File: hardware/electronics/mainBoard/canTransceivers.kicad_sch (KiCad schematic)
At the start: 20 parts, among them U6 TCAN3403-Q1, U7 TCAN3403-Q1

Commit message: assigned FPs
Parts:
- U6, U7: footprint (none) -> lib_ICs:SON65P300X300X100-8
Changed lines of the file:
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@@
 			)
 		)
-		(property "Footprint" ""
+		(property "Footprint" "lib_ICs:SON65P300X300X100-8"
 			(at 139.7 63.5 0)
 			(effects
@@
 			)
 		)
-		(property "Footprint" ""
+		(property "Footprint" "lib_ICs:SON65P300X300X100-8"
 			(at 139.7 127 0)
 			(effects

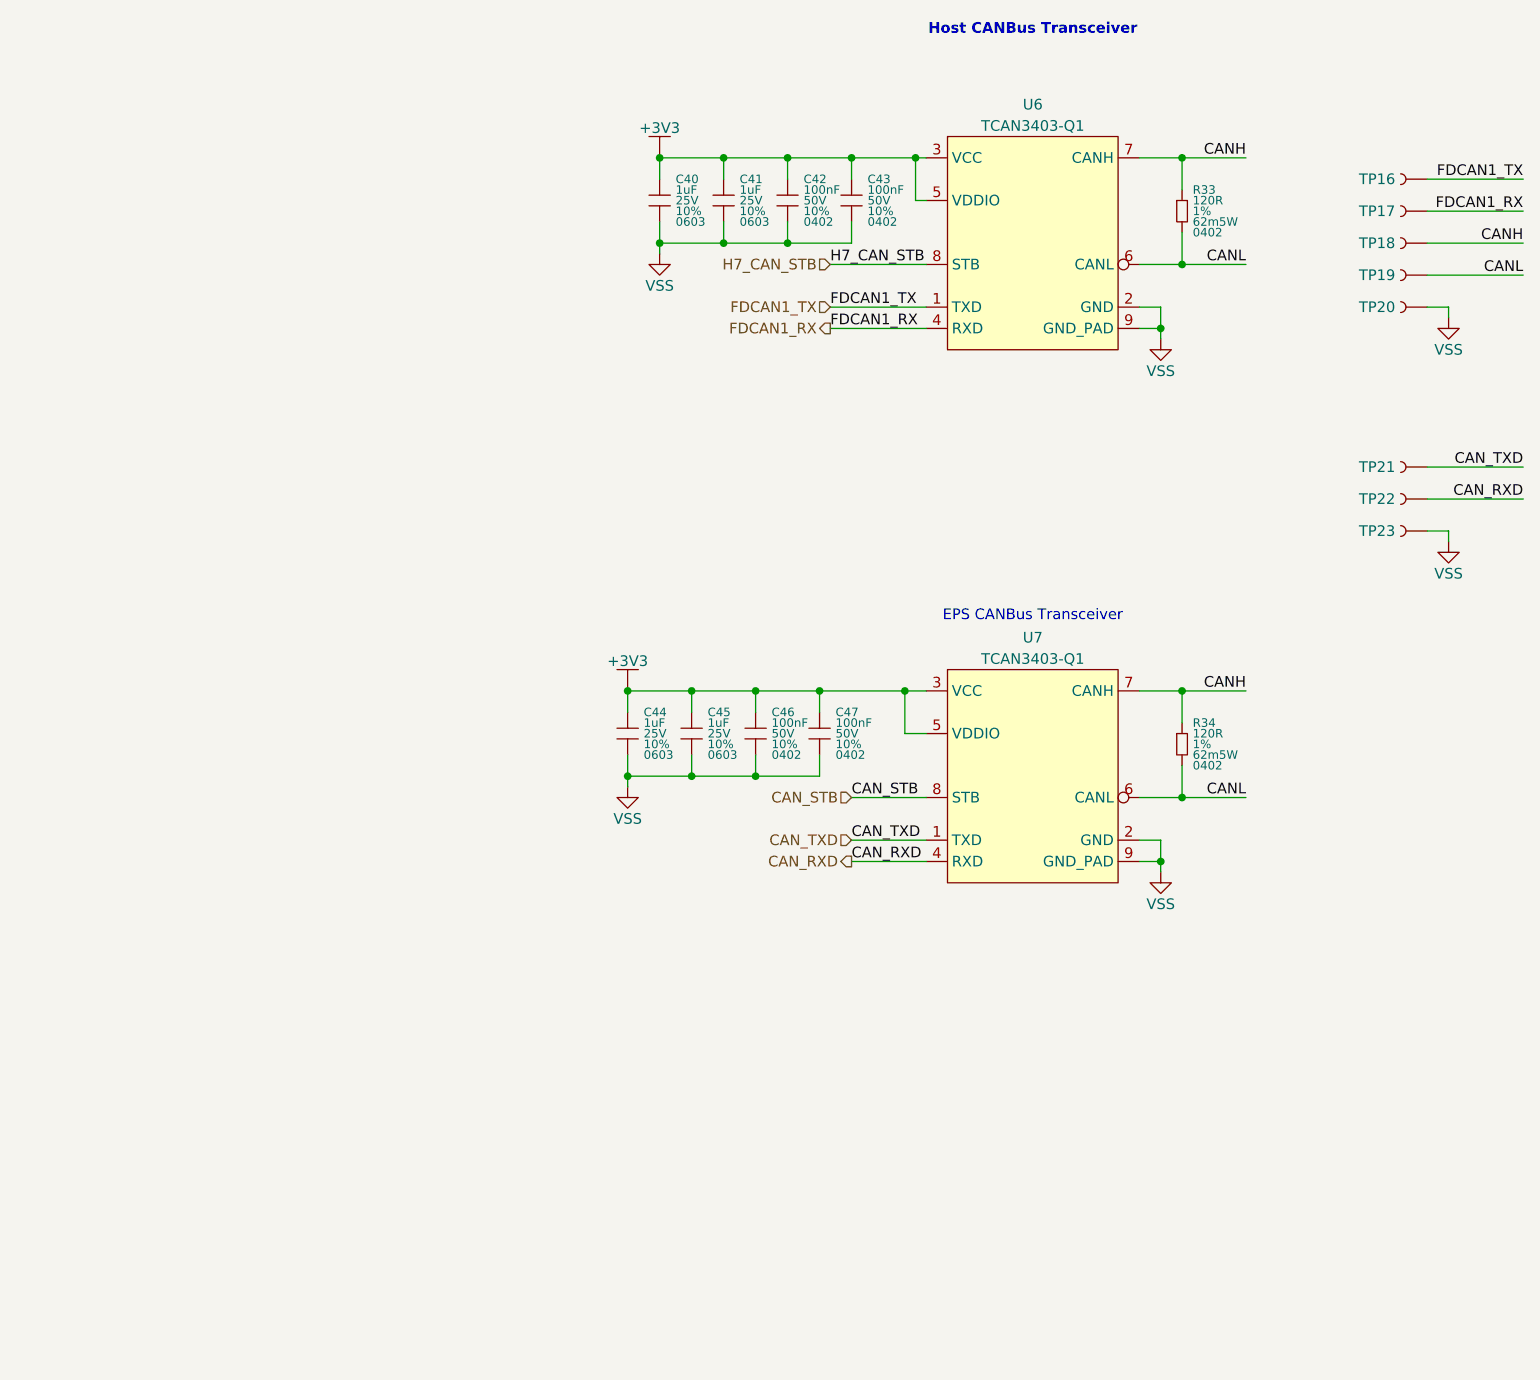
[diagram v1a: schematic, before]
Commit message: assigned footprints
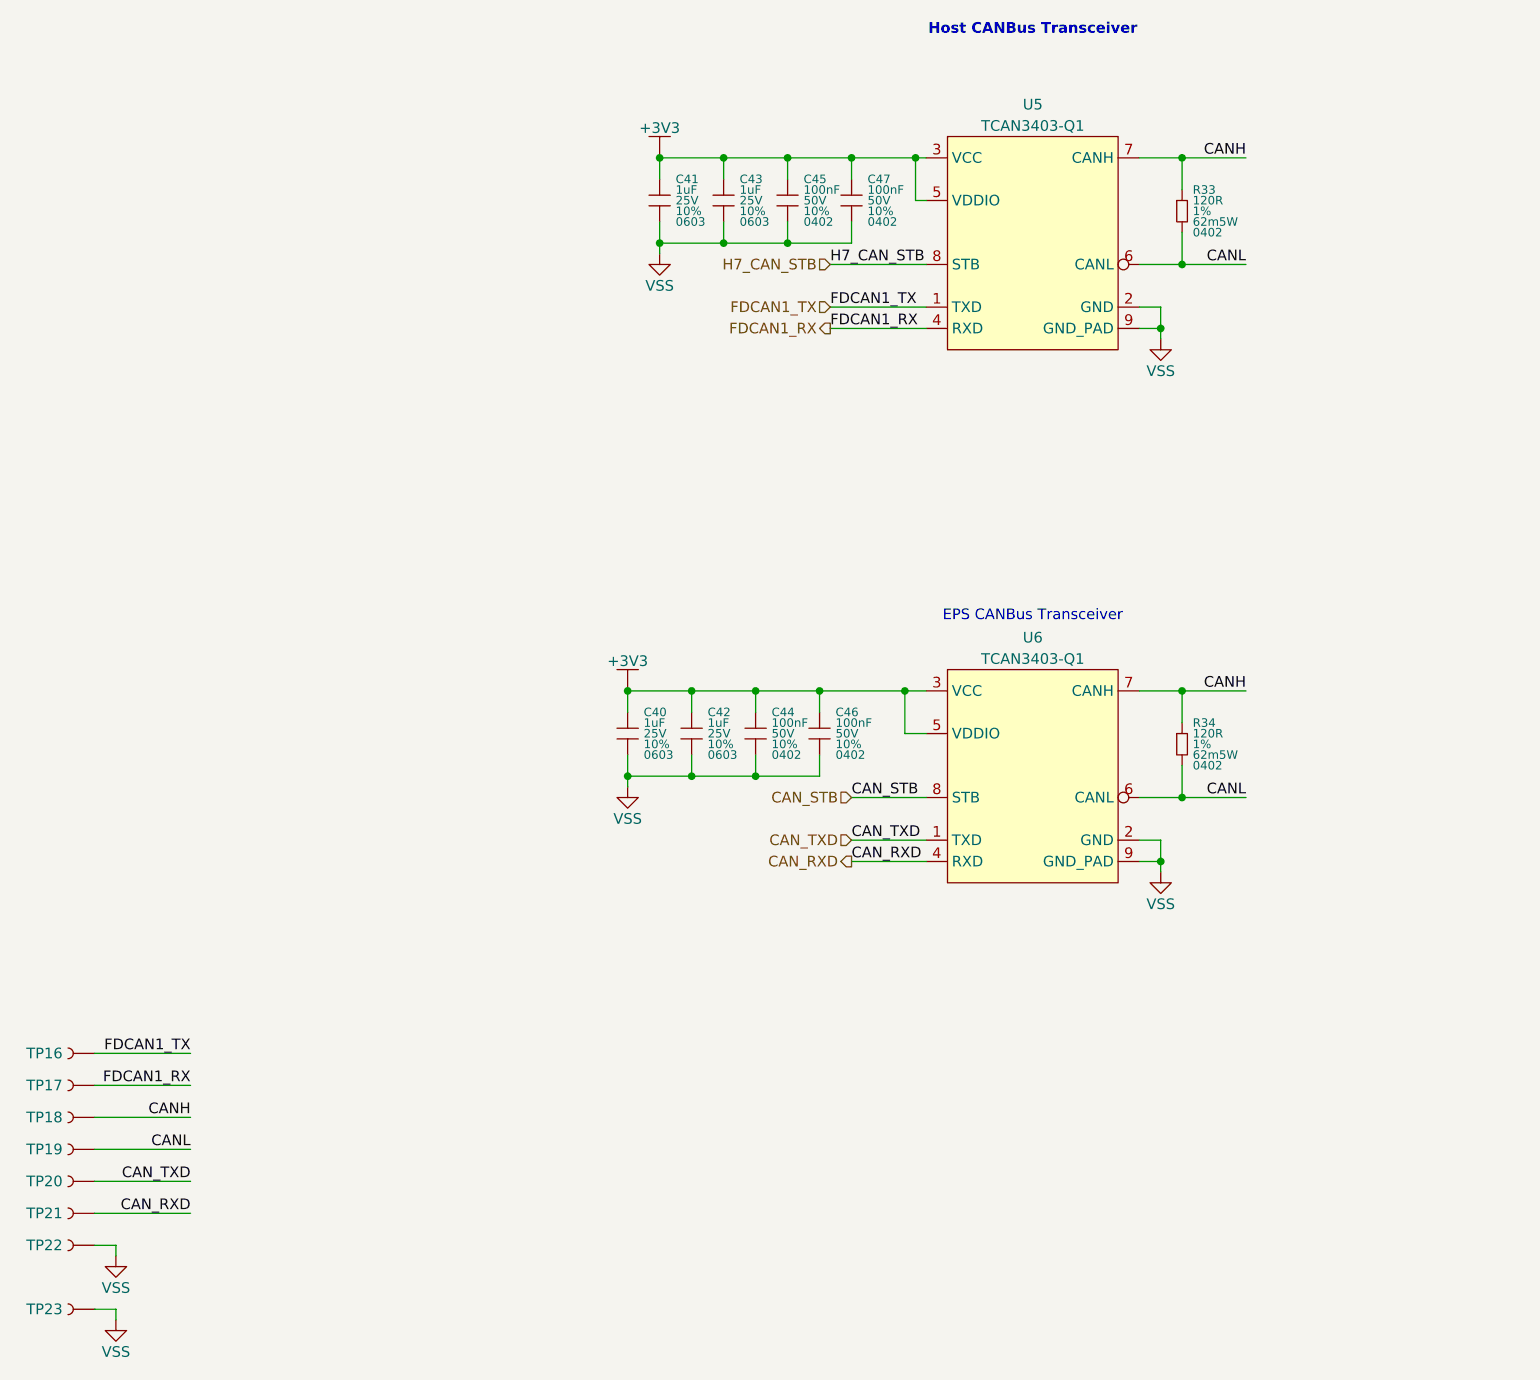
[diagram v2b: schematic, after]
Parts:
- C40: renamed from C44; footprint (none) -> lib_passives:GRT0603
- C41: renamed from C40; footprint (none) -> lib_passives:GRT0603
- C42: renamed from C45; footprint (none) -> lib_passives:GRT0603
- C43: renamed from C41; footprint (none) -> lib_passives:GRT0603
- C44: renamed from C46; footprint (none) -> lib_passives:GCM0402
- C45: renamed from C42; footprint (none) -> lib_passives:GCM0402
- C46: renamed from C47; footprint (none) -> lib_passives:GCM0402
- C47: renamed from C43; footprint (none) -> lib_passives:GCM0402
- R33, R34: footprint (none) -> lib_passives:CRCW0402
- TP16, TP17, TP18, TP19: footprint (none) -> lib_misc:TP_2mm
- TP20: renamed from TP21; footprint (none) -> lib_misc:TP_2mm
- TP21: renamed from TP22; footprint (none) -> lib_misc:TP_2mm
- TP22: renamed from TP20; footprint (none) -> lib_misc:TP_RCW
- TP23: footprint (none) -> lib_misc:TP_RCW
- renumbered U6 to U5, U7 to U6
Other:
- title: (none) -> CANBus Transceivers
- moved on the sheet: TP16, TP17, TP18, TP19, TP20, TP21, TP22, TP23

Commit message: assigned net classes
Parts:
- renumbered C41 to C40, C43 to C41, C45 to C42, C47 to C43, C40 to C44, C42 to C45, C44 to C46, C46 to C47
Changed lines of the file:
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@@
 	(wire
 		(pts
-			(xy 157.48 66.04) (xy 165.1 66.04)
+			(xy 157.48 66.04) (xy 177.8 66.04)
 		)
 		(stroke
@@
 	(wire
 		(pts
-			(xy 157.48 53.34) (xy 165.1 53.34)
+			(xy 157.48 53.34) (xy 177.8 53.34)
 		)
 		(stroke
@@
 	)
 	(label "CANL"
-		(at 165.1 66.04 180)
+		(at 177.8 66.04 180)
 		(effects
 			(font
@@
 	)
 	(label "CANH"
-		(at 165.1 53.34 180)
+		(at 177.8 53.34 180)
 		(effects
 			(font
@@
 		)
 	)
+	(rule_area
+		(polyline
+			(pts
+				(xy 165.1 52.07) (xy 165.1 67.31) (xy 167.64 67.31) (xy 167.64 52.07)
+			)
+			(stroke
+				(width 0)
+				(type dash)
+			)
+			(fill
+				(type none)
+			)
+		)
+	)
+	(netclass_flag ""
+		(length 2.54)
+		(shape round)
+		(at 166.37 52.07 0)
+		(fields_autoplaced yes)
+		(effects
+			(font
+				(size 1.27 1.27)
+			)
+			(justify left bottom)
+		)
+		(property "Netclass" "CANBus"
+			(at 167.0685 49.53 0)
+			(effects
+				(font
+					(size 1.27 1.27)
+				)
+				(justify left)
+			)
+		)
+		(property "Component Class" ""
+			(at -34.29 11.43 0)
+			(effects
+				(font
+					(size 1.27 1.27)
+					(italic yes)
+				)
+			)
+		)
+	)
 	(symbol
 		(lib_id "lib_sch:Testpoint")
@@
 		(dnp no)
 		(fields_autoplaced yes)
-		(property "Reference" "#PWR098"
+		(property "Reference" "#PWR0104"
 			(at 30.48 191.77 0)
 			(effects
@@
 			(project "mainBoard"
 				(path "/be16e32f-2ccf-4272-9ec7-94d5fe7a55e0/fe7c77e0-d375-4e15-a96c-a27be84d1fb8"
-					(reference "#PWR098")
+					(reference "#PWR0104")
 					(unit 1)
 				)
@@
 		(dnp no)
 		(fields_autoplaced yes)
-		(property "Reference" "#PWR099"
+		(property "Reference" "#PWR0100"
 			(at 91.44 116.84 0)
 			(effects
@@
 			(project "mainBoard"
 				(path "/be16e32f-2ccf-4272-9ec7-94d5fe7a55e0/fe7c77e0-d375-4e15-a96c-a27be84d1fb8"
-					(reference "#PWR099")
+					(reference "#PWR0100")
 					(unit 1)
 				)
@@
 		(dnp no)
 		(fields_autoplaced yes)
-		(property "Reference" "#PWR0101"
+		(property "Reference" "#PWR097"
 			(at 95.25 53.34 0)
 			(effects
@@
 			(project "mainBoard"
 				(path "/be16e32f-2ccf-4272-9ec7-94d5fe7a55e0/fe7c77e0-d375-4e15-a96c-a27be84d1fb8"
-					(reference "#PWR0101")
+					(reference "#PWR097")
 					(unit 1)
 				)
@@
 		(dnp no)
 		(fields_autoplaced yes)
-		(property "Reference" "C43"
+		(property "Reference" "C41"
 			(at 104.775 55.88 0)
 			(do_not_autoplace yes)
@@
 			(project "mainBoard"
 				(path "/be16e32f-2ccf-4272-9ec7-94d5fe7a55e0/fe7c77e0-d375-4e15-a96c-a27be84d1fb8"
-					(reference "C43")
+					(reference "C41")
 					(unit 1)
 				)
@@
 		(dnp no)
 		(fields_autoplaced yes)
-		(property "Reference" "C46"
+		(property "Reference" "C47"
 			(at 116.205 119.38 0)
 			(do_not_autoplace yes)
@@
 			(project "mainBoard"
 				(path "/be16e32f-2ccf-4272-9ec7-94d5fe7a55e0/fe7c77e0-d375-4e15-a96c-a27be84d1fb8"
-					(reference "C46")
+					(reference "C47")
 					(unit 1)
 				)
@@
 		(dnp no)
 		(fields_autoplaced yes)
-		(property "Reference" "#PWR0104"
+		(property "Reference" "#PWR0102"
 			(at 154.94 138.43 0)
 			(effects
@@
 			(project "mainBoard"
 				(path "/be16e32f-2ccf-4272-9ec7-94d5fe7a55e0/fe7c77e0-d375-4e15-a96c-a27be84d1fb8"
-					(reference "#PWR0104")
+					(reference "#PWR0102")
 					(unit 1)
 				)
@@
 		(dnp no)
 		(fields_autoplaced yes)
-		(property "Reference" "C45"
+		(property "Reference" "C42"
 			(at 112.395 55.88 0)
 			(do_not_autoplace yes)
@@
 			(project "mainBoard"
 				(path "/be16e32f-2ccf-4272-9ec7-94d5fe7a55e0/fe7c77e0-d375-4e15-a96c-a27be84d1fb8"
-					(reference "C45")
+					(reference "C42")
 					(unit 1)
 				)
@@
 		(dnp no)
 		(fields_autoplaced yes)
-		(property "Reference" "#PWR097"
+		(property "Reference" "#PWR0103"
 			(at 30.48 184.15 0)
 			(effects
@@
 			(project "mainBoard"
 				(path "/be16e32f-2ccf-4272-9ec7-94d5fe7a55e0/fe7c77e0-d375-4e15-a96c-a27be84d1fb8"
-					(reference "#PWR097")
+					(reference "#PWR0103")
 					(unit 1)
 				)
@@
 		(dnp no)
 		(fields_autoplaced yes)
-		(property "Reference" "C47"
+		(property "Reference" "C43"
 			(at 120.015 55.88 0)
 			(do_not_autoplace yes)
@@
 			(project "mainBoard"
 				(path "/be16e32f-2ccf-4272-9ec7-94d5fe7a55e0/fe7c77e0-d375-4e15-a96c-a27be84d1fb8"
-					(reference "C47")
+					(reference "C43")
 					(unit 1)
 				)
@@
 		(dnp no)
 		(fields_autoplaced yes)
-		(property "Reference" "#PWR0102"
+		(property "Reference" "#PWR098"
 			(at 95.25 64.77 0)
 			(effects
@@
 			(project "mainBoard"
 				(path "/be16e32f-2ccf-4272-9ec7-94d5fe7a55e0/fe7c77e0-d375-4e15-a96c-a27be84d1fb8"
-					(reference "#PWR0102")
+					(reference "#PWR098")
 					(unit 1)
 				)
@@
 		(dnp no)
 		(fields_autoplaced yes)
-		(property "Reference" "C41"
+		(property "Reference" "C40"
 			(at 97.155 55.88 0)
 			(do_not_autoplace yes)
@@
 			(project "mainBoard"
 				(path "/be16e32f-2ccf-4272-9ec7-94d5fe7a55e0/fe7c77e0-d375-4e15-a96c-a27be84d1fb8"
-					(reference "C41")
+					(reference "C40")
 					(unit 1)
 				)
@@
 		(dnp no)
 		(fields_autoplaced yes)
-		(property "Reference" "#PWR0103"
+		(property "Reference" "#PWR099"
 			(at 154.94 74.93 0)
 			(effects
@@
 			(project "mainBoard"
 				(path "/be16e32f-2ccf-4272-9ec7-94d5fe7a55e0/fe7c77e0-d375-4e15-a96c-a27be84d1fb8"
-					(reference "#PWR0103")
+					(reference "#PWR099")
 					(unit 1)
 				)
@@
 		(dnp no)
 		(fields_autoplaced yes)
-		(property "Reference" "#PWR0100"
+		(property "Reference" "#PWR0101"
 			(at 91.44 128.27 0)
 			(effects
@@
 			(project "mainBoard"
 				(path "/be16e32f-2ccf-4272-9ec7-94d5fe7a55e0/fe7c77e0-d375-4e15-a96c-a27be84d1fb8"
-					(reference "#PWR0100")
+					(reference "#PWR0101")
 					(unit 1)
 				)
@@
 		(dnp no)
 		(fields_autoplaced yes)
-		(property "Reference" "C42"
+		(property "Reference" "C45"
 			(at 100.965 119.38 0)
 			(do_not_autoplace yes)
@@
 			(project "mainBoard"
 				(path "/be16e32f-2ccf-4272-9ec7-94d5fe7a55e0/fe7c77e0-d375-4e15-a96c-a27be84d1fb8"
-					(reference "C42")
+					(reference "C45")
 					(unit 1)
 				)
@@
 		(dnp no)
 		(fields_autoplaced yes)
-		(property "Reference" "C44"
+		(property "Reference" "C46"
 			(at 108.585 119.38 0)
 			(do_not_autoplace yes)
@@
 			(project "mainBoard"
 				(path "/be16e32f-2ccf-4272-9ec7-94d5fe7a55e0/fe7c77e0-d375-4e15-a96c-a27be84d1fb8"
-					(reference "C44")
+					(reference "C46")
 					(unit 1)
 				)
@@
 		(dnp no)
 		(fields_autoplaced yes)
-		(property "Reference" "C40"
+		(property "Reference" "C44"
 			(at 93.345 119.38 0)
 			(do_not_autoplace yes)
@@
 			(project "mainBoard"
 				(path "/be16e32f-2ccf-4272-9ec7-94d5fe7a55e0/fe7c77e0-d375-4e15-a96c-a27be84d1fb8"
-					(reference "C40")
+					(reference "C44")
 					(unit 1)
 				)
